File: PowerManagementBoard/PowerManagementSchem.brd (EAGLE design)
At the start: 165.1 x 106.7 mm, 126 parts, among them J1 D15S24A4GV00LF, J8 182-037-213R531, J9 182-025-213R531, Q1 PMOSFET, Q10 PMOSFET, Q11 PMOSFET, Q12 PMOSFET, Q2 PMOSFET, Q3 PMOSFET, Q4 PMOSFET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

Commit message: Finished RPi board rev 2.
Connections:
- new net ANT-BUSY: J2.19
- new net ANT-BUSY_2: J3.20, J8.25
- net GND: no longer J8.25
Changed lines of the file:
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@@
 <contactref element="J8" pad="23"/>
 <contactref element="J8" pad="24"/>
-<contactref element="J8" pad="25"/>
 <contactref element="U12" pad="3"/>
 <contactref element="U11" pad="3"/>
 <contactref element="U10" pad="3"/>
+<wire x1="143.51" y1="81.28" x2="129.655" y2="103.02" width="0" layer="19" extent="1-1"/>
+<wire x1="105.156" y1="90.678" x2="129.655" y2="103.02" width="0" layer="19" extent="1-1"/>
+<wire x1="110.49" y1="73.66" x2="105.156" y2="90.678" width="0" layer="19" extent="1-1"/>
+<wire x1="82.779" y1="98.501" x2="105.156" y2="90.678" width="0" layer="19" extent="1-1"/>
+<wire x1="78.74" y1="100.01" x2="82.55" y2="100.33" width="0" layer="19" extent="1-1"/>
+<wire x1="77.216" y1="96.774" x2="78.74" y2="100.01" width="0" layer="19" extent="1-1"/>
+<wire x1="75.184" y1="96.774" x2="77.216" y2="96.774" width="0" layer="19" extent="1-1"/>
+<wire x1="73.66" y1="100.01" x2="75.054" y2="96.774" width="0" layer="19" extent="1-1"/>
+<wire x1="65.125" y1="99.06" x2="73.66" y2="100.01" width="0" layer="19" extent="1-1"/>
+<wire x1="73.66" y1="86.36" x2="73.66" y2="95.38" width="0" layer="19" extent="1-1"/>
+<wire x1="57.658" y1="90.678" x2="65.125" y2="99.06" width="0" layer="19" extent="1-1"/>
+<wire x1="45.15" y1="100.18" x2="57.658" y2="90.678" width="0" layer="19" extent="1-1"/>
+<wire x1="42.41" y1="100.18" x2="45.15" y2="100.18" width="0" layer="19" extent="1-1"/>
+<wire x1="39.67" y1="100.18" x2="42.41" y2="100.18" width="0" layer="19" extent="1-1"/>
+<wire x1="36.93" y1="100.18" x2="39.67" y2="100.18" width="0" layer="19" extent="1-1"/>
+<wire x1="43.78" y1="103.02" x2="45.15" y2="100.18" width="0" layer="19" extent="1-1"/>
+<wire x1="41.04" y1="103.02" x2="43.78" y2="103.02" width="0" layer="19" extent="1-1"/>
+<wire x1="38.3" y1="103.02" x2="41.04" y2="103.02" width="0" layer="19" extent="1-1"/>
+<wire x1="35.56" y1="103.02" x2="38.3" y2="103.02" width="0" layer="19" extent="1-1"/>
+<wire x1="29.21" y1="86.36" x2="36.93" y2="100.18" width="0" layer="19" extent="1-1"/>
+<wire x1="20.066" y1="90.678" x2="29.21" y2="86.36" width="0" layer="19" extent="1-1"/>
+<wire x1="13.462" y1="93.98" x2="20.066" y2="90.678" width="0" layer="19" extent="1-1"/>
+<wire x1="1.778" y1="90.932" x2="13.462" y2="93.98" width="0" layer="19" extent="1-1"/>
+<wire x1="1.905" y1="80.515" x2="1.905" y2="88.395" width="0" layer="19" extent="1-1"/>
+<wire x1="4.064" y1="48.006" x2="1.778" y2="78.74" width="0" layer="19" extent="1-1"/>
+<wire x1="4.064" y1="28.702" x2="3.363" y2="47.305" width="0" layer="19" extent="1-1"/>
+<wire x1="4.13" y1="19.05" x2="4.13" y2="21.59" width="0" layer="19" extent="1-1"/>
+<wire x1="11.11" y1="24.13" x2="4.13" y2="24.13" width="0" layer="19" extent="1-1"/>
+<wire x1="14.224" y1="19.05" x2="14.478" y2="24.13" width="0" layer="19" extent="1-1"/>
+<wire x1="11.11" y1="13.97" x2="11.11" y2="19.05" width="0" layer="19" extent="1-1"/>
+<wire x1="19.05" y1="5.08" x2="15.494" y2="13.97" width="0" layer="19" extent="1-1"/>
+<wire x1="27.255" y1="3.66" x2="19.05" y2="5.08" width="0" layer="19" extent="1-1"/>
+<wire x1="30.025" y1="3.66" x2="27.255" y2="3.66" width="0" layer="19" extent="1-1"/>
+<wire x1="32.795" y1="3.66" x2="30.025" y2="3.66" width="0" layer="19" extent="1-1"/>
+<wire x1="35.565" y1="3.66" x2="32.795" y2="3.66" width="0" layer="19" extent="1-1"/>
+<wire x1="38.335" y1="3.66" x2="35.565" y2="3.66" width="0" layer="19" extent="1-1"/>
+<wire x1="31.75" y1="40.64" x2="14.478" y2="24.13" width="0" layer="19" extent="1-1"/>
+<wire x1="135.89" y1="50.8" x2="143.51" y2="81.28" width="0" layer="19" extent="1-1"/>
+<wire x1="139.446" y1="38.0238" x2="135.89" y2="50.8" width="0" layer="19" extent="1-1"/>
+<wire x1="139.7" y1="26.8478" x2="139.446" y2="36.83" width="0" layer="19" extent="1-1"/>
+<wire x1="139.7" y1="14.9098" x2="139.7" y2="25.654" width="0" layer="19" extent="1-1"/>
+<wire x1="151.19" y1="33.655" x2="139.446" y2="36.83" width="0" layer="19" extent="1-1"/>
+<wire x1="153.035" y1="32.385" x2="153.035" y2="33.655" width="0" layer="19" extent="1-1"/>
+<wire x1="153.162" y1="21.082" x2="153.162" y2="32.258" width="0" layer="19" extent="1-1"/>
+<wire x1="153.035" y1="19.685" x2="153.035" y2="20.955" width="0" layer="19" extent="1-1"/>
+<wire x1="151.13" y1="48.26" x2="151.19" y2="33.655" width="0" layer="19" extent="1-1"/>
+<wire x1="116.459" y1="4.953" x2="139.7" y2="13.716" width="0" layer="19" extent="1-16"/>
 </signal>
 <signal name="12V-CTRL">
@@
 <wire x1="153.797" y1="29.845" x2="153.924" y2="29.972" width="0.254" layer="1"/>
 </signal>
+<signal name="ANT-BUSY">
+<contactref element="J2" pad="19"/>
+</signal>
+<signal name="ANT-BUSY_2">
+<contactref element="J3" pad="20"/>
+<contactref element="J8" pad="25"/>
+<wire x1="41.105" y1="3.66" x2="114.3" y2="6.223" width="0" layer="19" extent="1-1"/>
+</signal>
 </signals>

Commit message: Moved some files around. Made progress on power management board
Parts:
- added JP1, JP2: JUMPER-SMT_2_NO_NO-SILK, SparkFun-Jumpers:SMT-JUMPER_2_NO_NO-SILK
- added TP10, TP11, TP12, TP13, TP14, TP15, TP16: TPPAD1-13, testpad:P1-13
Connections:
- removed net VIN: U8.VIN
- new net N$2: TP10.TP, U8.8
- new net N$3: TP11.TP, U8.9
- new net N$33: TP15.TP, U8.10
- new net N$35: TP16.TP, U8.18
- new net N$37: JP1.1, U8.VIN
- new net N$38: JP2.1, U8.3.3V
- new net N$4: TP12.TP, U8.13
- new net N$6: TP13.TP, U8.12
- new net N$7: TP14.TP, U8.11
- net MNGR-3.3V: now also JP2.2; no longer U8.3.3V
- net MNGR-5V: now also JP1.2
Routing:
- net MNGR-5V: track 28.3 -> 106.6 mm, vias 0 -> 2
- net N$35: track 0.00 -> 7.40 mm
- net N$2: track 0.00 -> 6.81 mm
- net N$7: track 0.00 -> 6.66 mm
- net N$33: track 0.00 -> 6.66 mm
- net N$3: track 0.00 -> 6.66 mm
- net N$37: track 0.00 -> 3.40 mm
- net N$6: track 0.00 -> 2.54 mm
- net N$38: track 0.00 -> 2.13 mm
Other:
- board text added: "Teensy 3.3V"
- board text added: "Teensy 5V"

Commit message: Gerbers for RPi board made
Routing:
- net ANT-BUSY_2: track 0.00 -> 78.2 mm, vias 0 -> 1
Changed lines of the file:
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@@
 <contactref element="J3" pad="20"/>
 <contactref element="J8" pad="25"/>
-<wire x1="41.105" y1="3.66" x2="114.3" y2="6.223" width="0" layer="19" extent="1-1"/>
+<wire x1="41.105" y1="3.66" x2="42.271" y2="4.826" width="0.254" layer="16"/>
+<wire x1="74.93" y1="4.826" x2="75.692" y2="4.064" width="0.254" layer="16"/>
+<wire x1="79.0181875" y1="3.9243" x2="79.6810125" y2="3.9243" width="0.254" layer="16"/>
+<wire x1="80.1868" y1="6.058875" x2="81.571125" y2="7.4432" width="0.254" layer="16"/>
+<wire x1="78.8784875" y1="4.064" x2="79.0181875" y2="3.9243" width="0.254" layer="16"/>
+<wire x1="79.6810125" y1="3.9243" x2="80.1868" y2="4.4300875" width="0.254" layer="16"/>
+<wire x1="80.1868" y1="4.4300875" x2="80.1868" y2="6.058875" width="0.254" layer="16"/>
+<wire x1="75.692" y1="4.064" x2="78.8784875" y2="4.064" width="0.254" layer="16"/>
+<wire x1="83.528875" y1="7.4432" x2="84.6020375" y2="6.3700375" width="0.254" layer="16"/>
+<wire x1="84.6020375" y1="6.3700375" x2="89.53698125" y2="6.3700375" width="0.254" layer="16"/>
+<wire x1="89.53698125" y1="6.3700375" x2="90.91394375" y2="7.747" width="0.254" layer="16"/>
+<wire x1="107.823" y1="7.747" x2="107.95" y2="7.62" width="0.254" layer="16"/>
+<via x="107.95" y="7.62" extent="1-16" drill="0.35"/>
+<wire x1="107.95" y1="7.62" x2="111.10694375" y2="7.62" width="0.254" layer="1"/>
+<wire x1="111.10694375" y1="7.62" x2="111.23394375" y2="7.747" width="0.254" layer="1"/>
+<wire x1="111.23394375" y1="7.747" x2="112.776" y2="7.747" width="0.254" layer="1"/>
+<wire x1="112.776" y1="7.747" x2="114.3" y2="6.223" width="0.254" layer="1"/>
+<wire x1="42.271" y1="4.826" x2="74.93" y2="4.826" width="0.254" layer="16"/>
+<wire x1="81.571125" y1="7.4432" x2="83.528875" y2="7.4432" width="0.254" layer="16"/>
+<wire x1="90.91394375" y1="7.747" x2="107.823" y2="7.747" width="0.254" layer="16"/>
 </signal>
 <signal name="N$2">

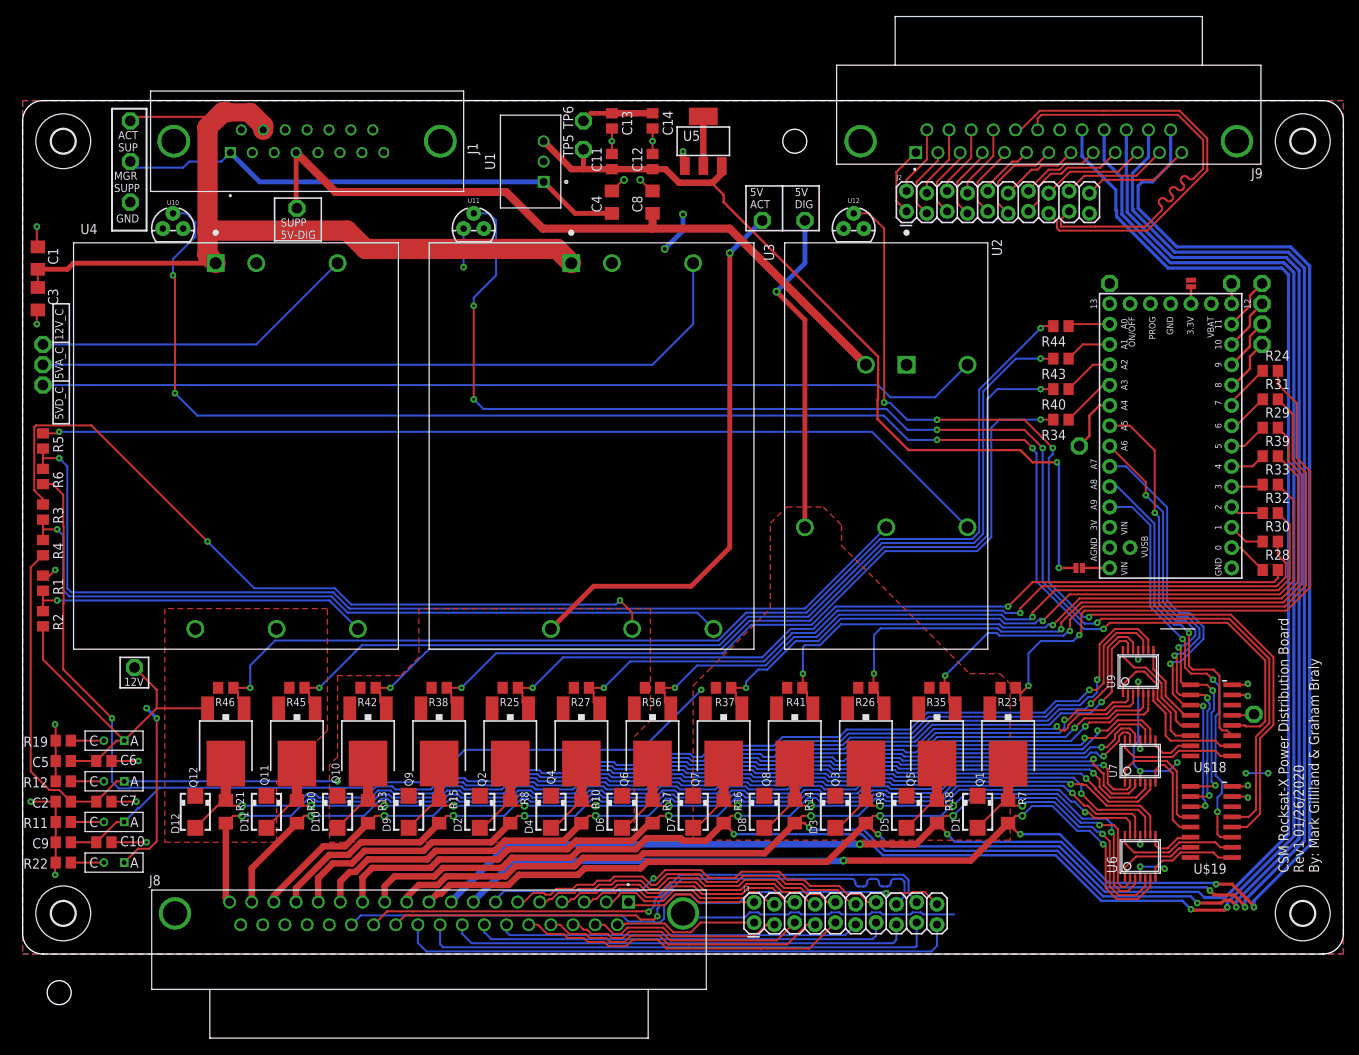
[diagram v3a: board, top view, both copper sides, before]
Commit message: Implemented ANT-BUSY signal to replace 5V supply on lidar
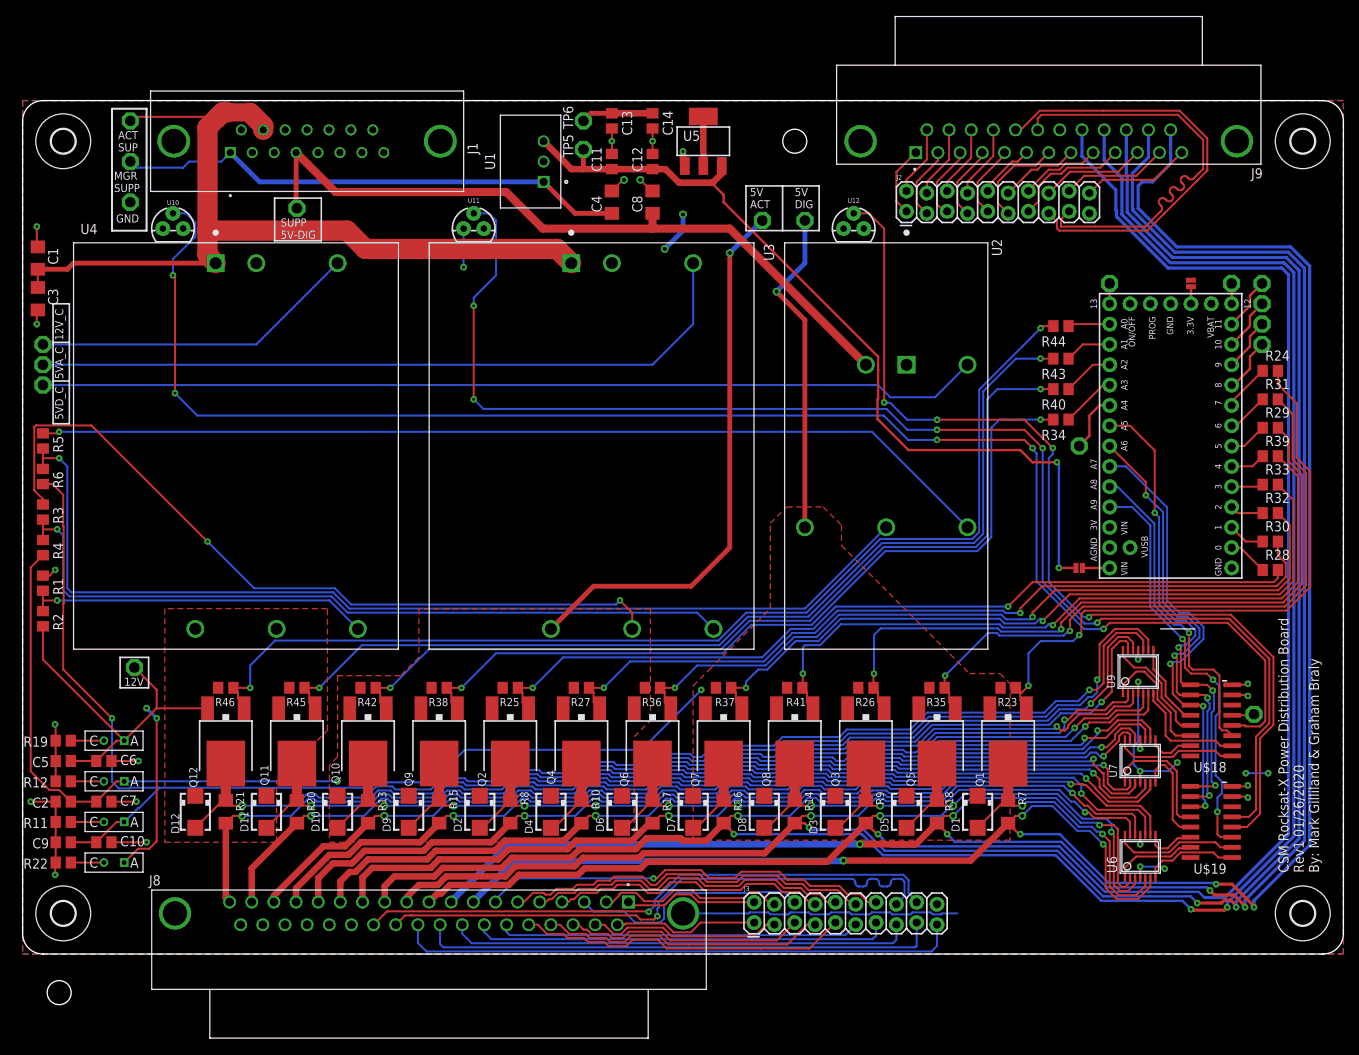
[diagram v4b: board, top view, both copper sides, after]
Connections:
- removed net LASER-UART-3: J2.5, J9.3
- removed net LASER-UART-3_2: J3.6, J8.3
- net ANT-BUSY: now also J2.5, J9.3; no longer J2.19
- net ANT-BUSY_2: now also J3.6, J8.3; no longer J3.20, J8.25
- net GND: now also J8.25
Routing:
- net ANT-BUSY_2: track 78.2 -> 30.5 mm, vias 1 -> 0
- net LASER-UART-3_2: track 29.5 -> 0.00 mm
- net ANT-BUSY: track 0.00 -> 9.29 mm
- net LASER-UART-3: track 9.07 -> 0.00 mm
- net N$4: track 0.00 -> 2.54 mm

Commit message: Made a nice silkscreen for power board
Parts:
- removed H5: MOUNT-HOLE3.0, holes:3,0
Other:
- board text added: "12V CAM"
- board text added: "12V STA"
- board text added: "5VA"
- board text added: "5VA CAM"
- board text added: "5VA LAS"
- board text added: "5VA MAG"
- board text added: "5VA STA"
- board text added: "5VA TX"
- board text added: "5VD"
- board text added: "5VD CAM"
- board text added: "5VD LAS"
- board text added: "5VD MAG"
- board text added: "5VD STA"
- board text added: "5VD TX"
- board text added: "MNGR"
